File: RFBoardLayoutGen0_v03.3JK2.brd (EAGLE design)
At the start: 76.9 x 40.1 mm, 79 parts

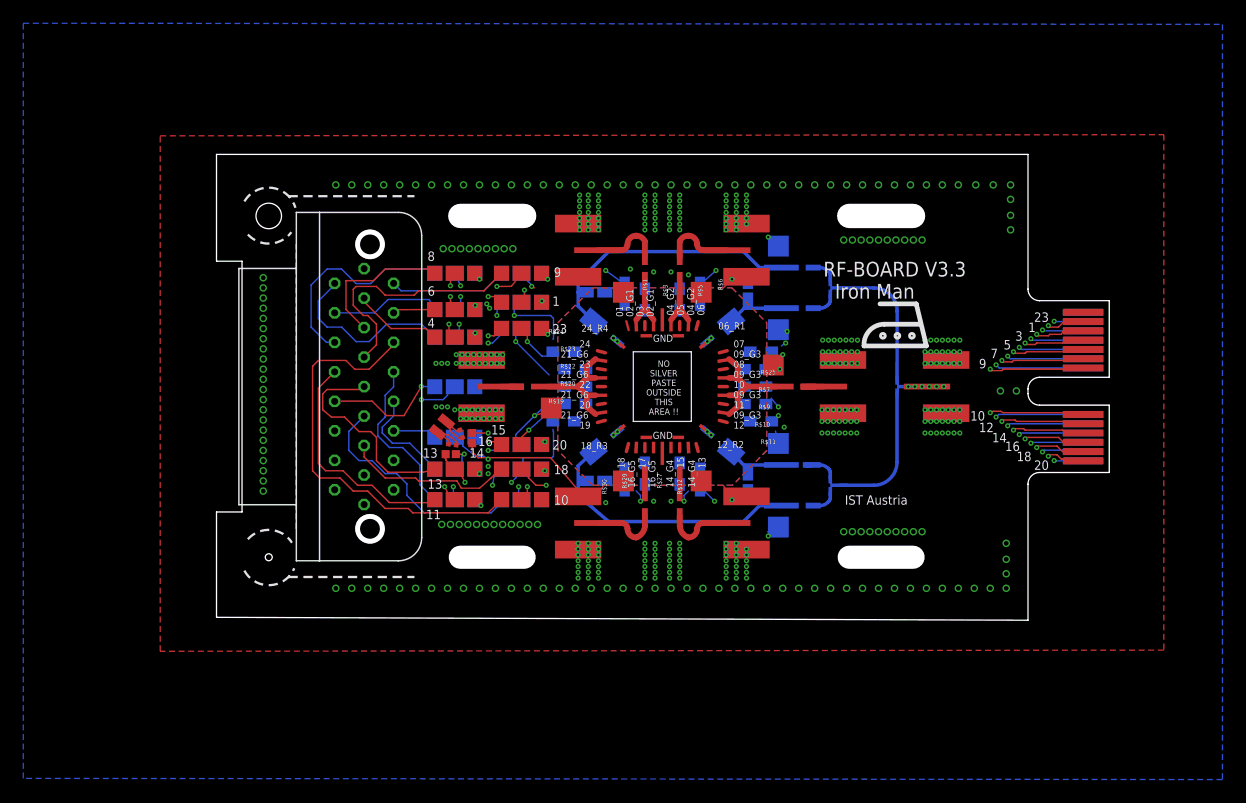
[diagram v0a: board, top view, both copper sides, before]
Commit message: moving border vias
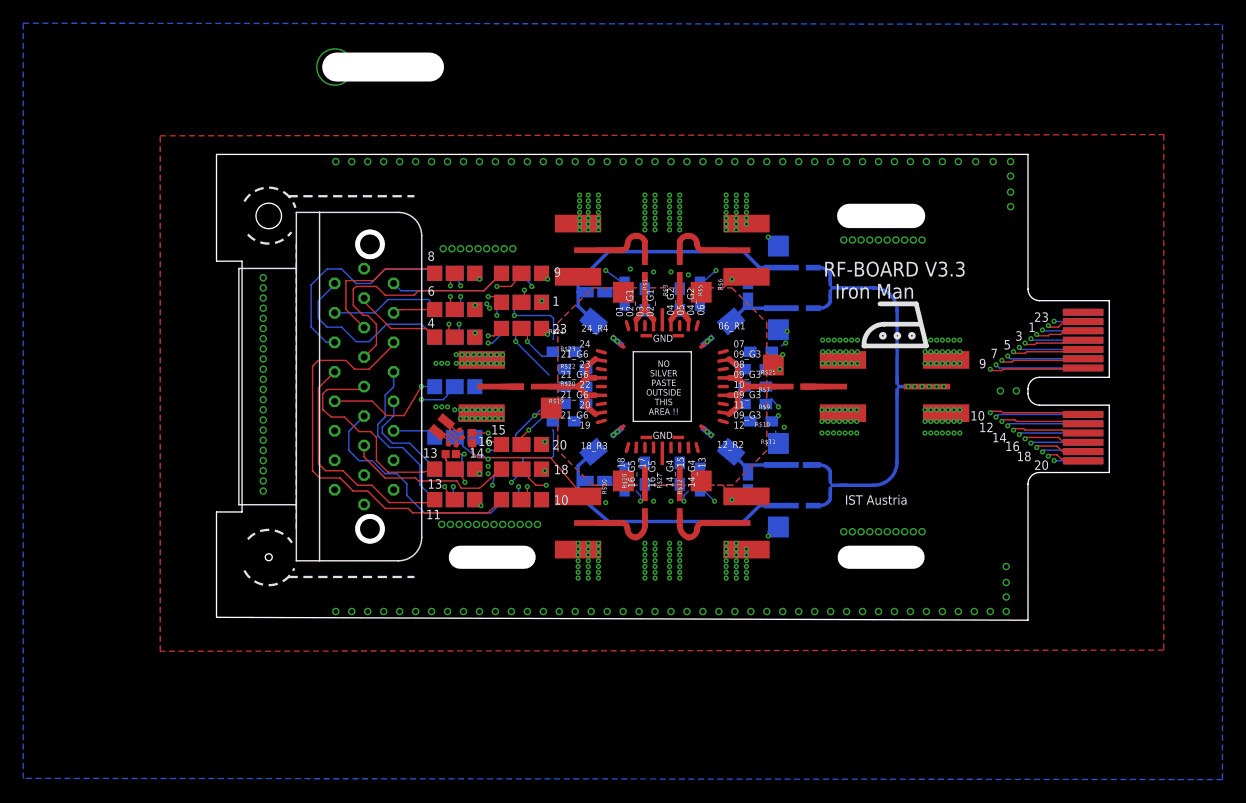
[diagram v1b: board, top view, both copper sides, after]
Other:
- board size 76.9 x 40.1 mm -> 76.9 x 47.6 mm

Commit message: added holes for blue fors
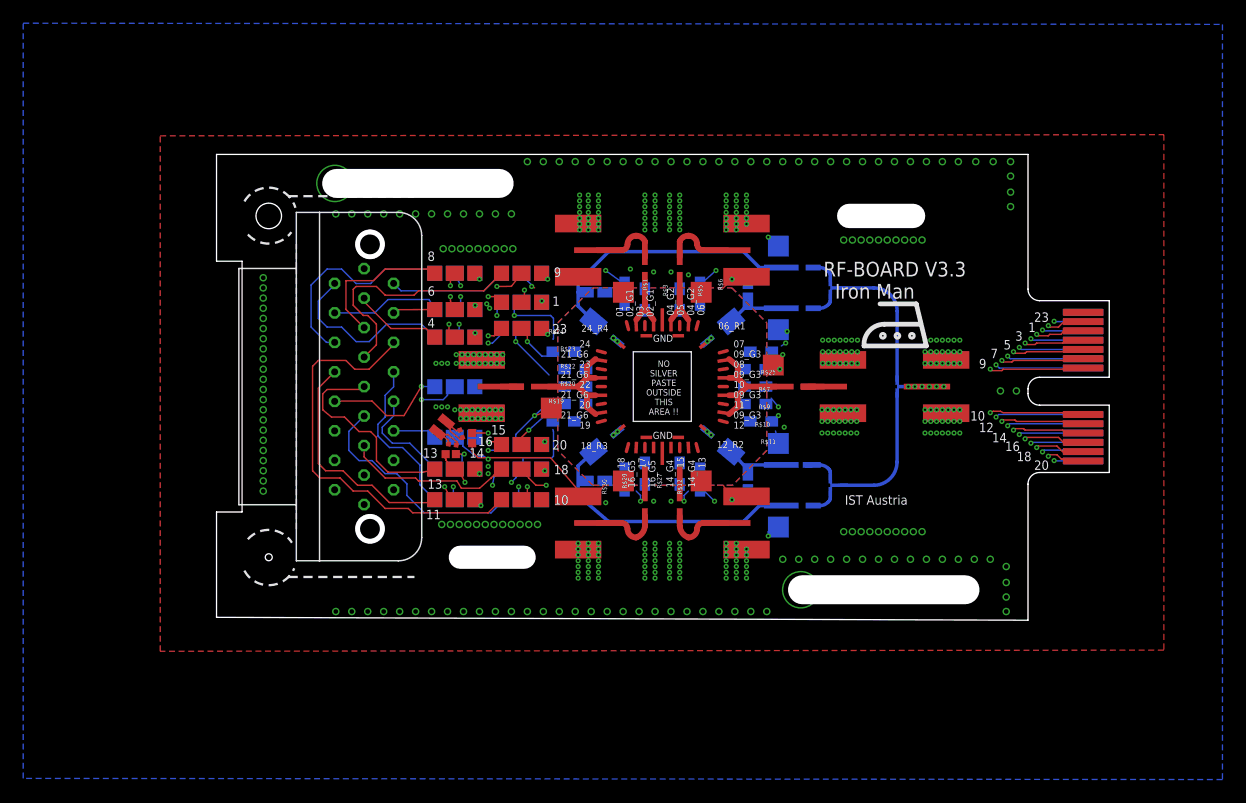
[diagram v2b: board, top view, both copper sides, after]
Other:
- board size 76.9 x 47.6 mm -> 76.9 x 40.1 mm
- board text added: "tell beta to put Cu on walls here"

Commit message: back two holes added
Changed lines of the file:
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@@
 <text x="-23.95" y="5.45" size="0.8128" layer="22" font="vector" ratio="15" rot="MR180">10</text>
 <text x="-26.5" y="1.6" size="0.8128" layer="22" font="vector" ratio="15" rot="MR180">13</text>
-<circle x="-33.9" y="14.7" radius="2" width="0" layer="29"/>
-<circle x="-33.9" y="-14.7" radius="2" width="0" layer="29"/>
 <wire x1="-36" y1="15.95" x2="-31.6" y2="15.4" width="0.2" layer="21" style="dashdot" curve="-133.254829"/>
 <wire x1="-35.7" y1="13.1" x2="-31.95" y2="13.3" width="0.2" layer="21" style="dashdot" curve="100.804892"/>
@@
 <circle x="-25.18125" y="-12.25" radius="1.05625" width="0.4064" layer="20"/>
 <circle x="-25.18125" y="12.25" radius="1.05625" width="0.4064" layer="20"/>
-<hole x="-33.9" y="-14.7" drill="0.6"/>
-<hole x="-33.9" y="14.7" drill="2.2"/>
 <wire x1="11.2" y1="13.29375" x2="12.64375" y2="11.39375" width="0.3048" layer="100"/>
 <wire x1="-7.70625" y1="13.3" x2="-10.275" y2="10.4" width="0.3048" layer="100"/>
@@
 <via x="29.625" y="-16.875" extent="1-16" drill="0.4"/>
 <via x="29.625" y="-15.5" extent="1-16" drill="0.4"/>
+<via x="-33.9" y="14.7" extent="1-16" drill="2.1" diameter="4"/>
 <wire x1="-10.4" y1="5.01" x2="-10.4" y2="5.01" width="0" layer="19" extent="1-16"/>
 <wire x1="-16.15" y1="-9.74" x2="-16.15" y2="-9.74" width="0" layer="19" extent="1-16"/>
+<via x="-33.9" y="-14.7" extent="1-16" drill="2.1" diameter="4"/>
 </signal>
 <signal name="N$5" class="2">
@@
 <via x="-28.2" y="17.5" extent="1-16" drill="3"/>
 <via x="-14.1" y="17.5" extent="1-16" drill="2.1"/>
+<wire x1="-14.1" y1="17.5" x2="-28.2" y2="17.5" width="0" layer="19" extent="1-1"/>
 </signal>
 <signal name="GND2">
 <via x="11.925" y="-17.5" extent="1-16" drill="3"/>
 <via x="26.025" y="-17.5" extent="1-16" drill="2.1"/>
+<wire x1="11.925" y1="-17.5" x2="26.025" y2="-17.5" width="0" layer="19" extent="1-1"/>
 </signal>
 </signals>

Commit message: Backup commit
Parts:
- added U$11, U$12, U$13, U$14: LP-FILTER/VARACTOR/0402, LPFilter:LP-FILTER/VARACTOR/0402
- moved R$27 1.50 mm to (0.00, -7.50)
- moved R$5 1.50 mm to (0.00, 7.50)
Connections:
- removed net $1234567254654: E$2.25, LP$1.$6, LP$10.$6, LP$11.$6, LP$12.$6, LP$13.$6, LP$14.$6, LP$15.$6, LP$16.$6, LP$17.$6, LP$18.$6, LP$19.$6, LP$2.$6, LP$20.$6, LP$21.$6, LP$22.$6, LP$23.$6, LP$24.$6, LP$3.$6, LP$4.$6, LP$5.$6, LP$6.$6, LP$7.$6, LP$8.$6, LP$9.$6, S$1.2@1, S$1.2@2, S$2.2@1, S$2.2@2, S$3.2@1, S$3.2@2, S$4.2@1, S$4.2@2, S$5.2@1, S$5.2@2, S$6.2@1, S$6.2@2, S$7.2@1, S$7.2@2, U$1.25, U$1.26
- net GND: now also E$2.25, LP$1.$6, LP$10.$6, LP$11.$6, LP$12.$6, LP$13.$6, LP$14.$6, LP$15.$6, LP$16.$6, LP$17.$6, LP$18.$6, LP$19.$6, LP$2.$6, LP$20.$6, LP$21.$6, LP$22.$6, LP$23.$6, LP$24.$6, LP$3.$6, LP$4.$6, LP$5.$6, LP$6.$6, LP$7.$6, LP$8.$6, LP$9.$6, S$1.2@1, S$1.2@2, S$2.2@1, S$2.2@2, S$3.2@1, S$3.2@2, S$4.2@1, S$4.2@2, S$5.2@1, S$5.2@2, S$6.2@1, S$6.2@2, S$7.2@1, S$7.2@2, U$1.25, U$1.26
- net N$10: now also U$14.IN
- net N$11: now also U$13.IN
- net N$2: now also U$12.IN
- net N$9: now also U$11.IN
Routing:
- added copper zone on layer 1, net GND
- added copper zone on layer 14, net GND
- added copper zone on layer 15, net GND
- added copper zone on layer 16, net GND
- added copper zone on layer 2, net GND
- added copper zone on layer 3, net GND
- removed copper zone on layer 1, net $1234567254654
- removed copper zone on layer 14, net $1234567254654
- removed copper zone on layer 15, net $1234567254654
- removed copper zone on layer 16, net $1234567254654
- removed copper zone on layer 2, net $1234567254654
- removed copper zone on layer 3, net $1234567254654

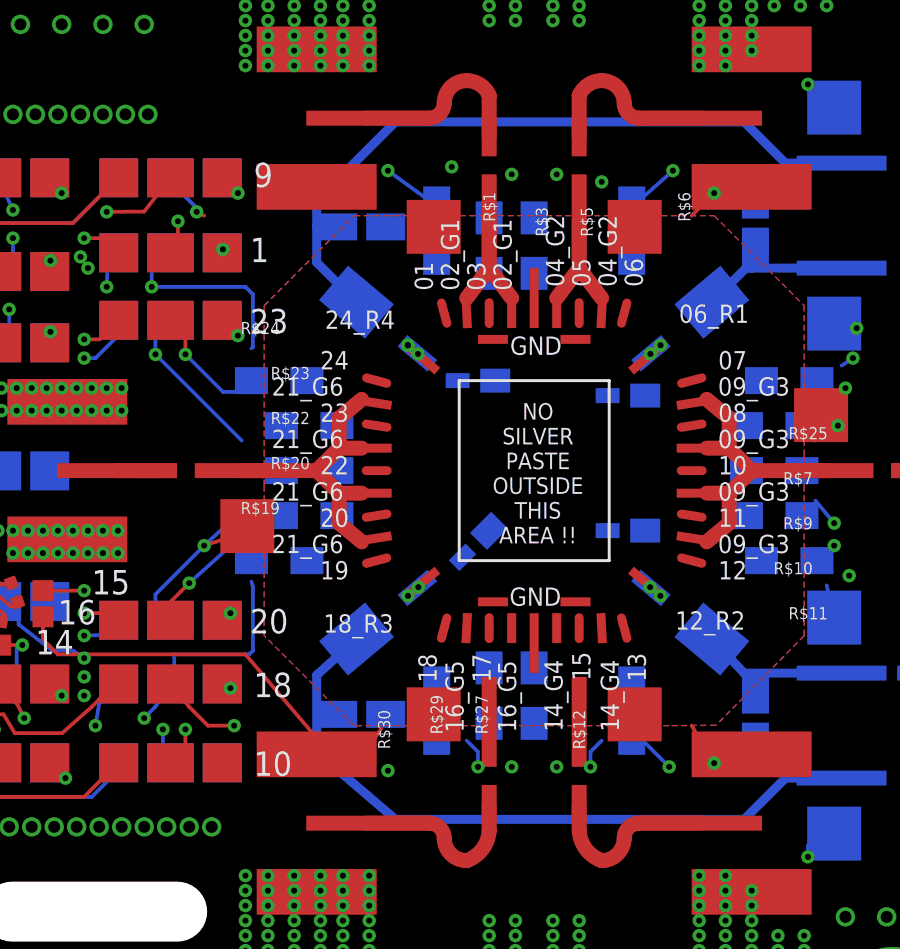
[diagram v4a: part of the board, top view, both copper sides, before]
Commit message: varactors added - problem spotted
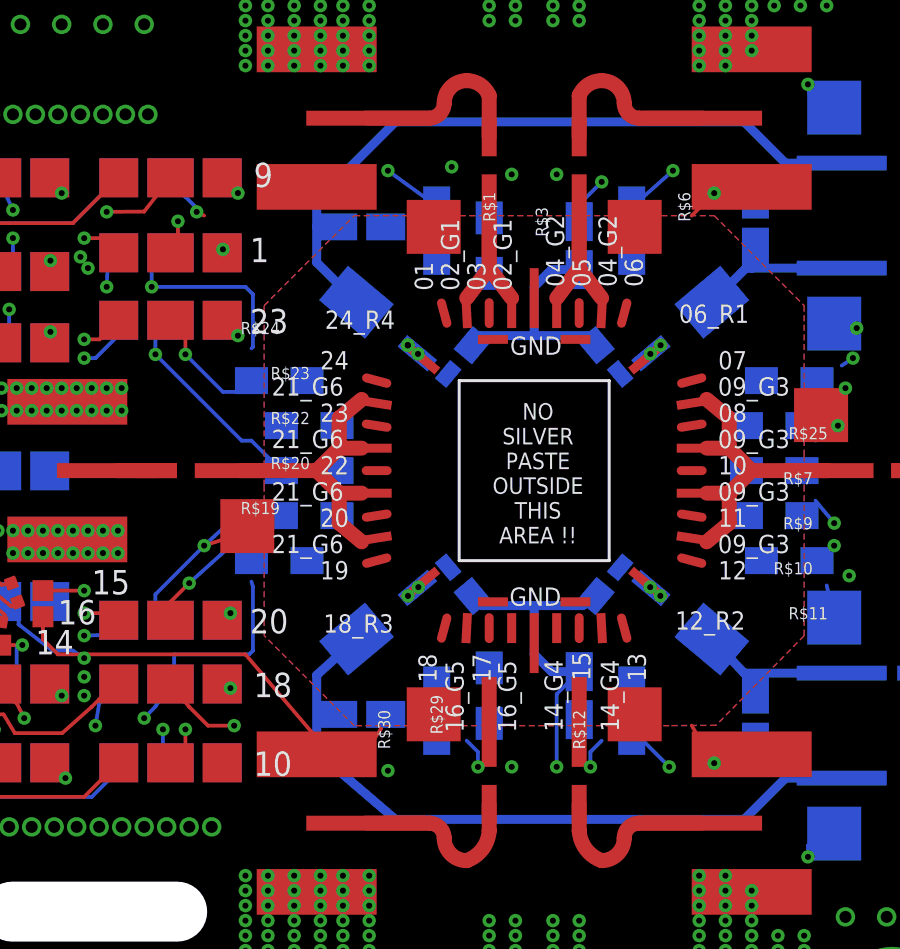
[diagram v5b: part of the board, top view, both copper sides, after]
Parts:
- removed R$27, R$5: 10K, LPFilter:LP-FILTER/RESISTOR/0603_BOTTOM
- added U$15, U$16: LP-FILTER/CAPACITOR/0603, LPFilter:LP-FILTER/CAPACITOR/0603_BOTTOM
- moved U$12 1.71 mm to (2.51, -3.64), turned to 230 degrees
- moved U$11 1.25 mm to (-2.51, -3.64), turned to 310 degrees
- moved U$13 1.24 mm to (2.51, 3.64), turned to 130 degrees
- moved U$14 0.82 mm to (-2.51, 3.64), turned to 50 degrees
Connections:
- removed net DC$15: R$27.OUT, U$6.DC§15
- removed net N$29: R$5.OUT, U$6.DC§05
- net D$15: now also U$11.OUT, U$12.OUT, U$16.OUT; no longer R$27.IN
- net D$5: now also U$13.OUT, U$14.OUT, U$15.OUT; no longer R$5.IN
- net GND: now also U$15.IN, U$16.IN
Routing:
- net D$15: track 70.2 -> 81.5 mm
- net D$5: track 65.4 -> 74.8 mm
- net D$22: track 61.9 -> 63.6 mm

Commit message: Routing
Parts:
- moved R$20 0.50 mm to (-8.00, -1.50)
- moved R$22 0.50 mm to (-8.00, 0.00)
- moved R$23 0.50 mm to (-8.00, 1.50)
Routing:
- net D$16: track 75.5 -> 69.1 mm, vias 3 -> 4
- net N$8: track 0.00 -> 5.12 mm
- net N$7: track 0.00 -> 5.12 mm
- net N$4: track 0.00 -> 2.43 mm, vias 0 -> 1
- net DC$24: track 0.00 -> 2.43 mm, vias 0 -> 1
- net DC$19: track 0.00 -> 2.43 mm, vias 0 -> 1
- net N$28: track 0.00 -> 2.39 mm, vias 0 -> 1
- net D$8: track 75.9 -> 78.1 mm
- net D$2: track 53.8 -> 55.8 mm
- net DC$6: track 0.00 -> 1.87 mm, vias 0 -> 1
- net DC$1: track 0.00 -> 1.87 mm, vias 0 -> 1
- net N$31: track 0.00 -> 1.86 mm, vias 0 -> 1
- net DC$13: track 0.00 -> 1.86 mm, vias 0 -> 1
- net N$33: track 0.00 -> 1.83 mm, vias 0 -> 1
- net N$32: track 0.00 -> 1.83 mm, vias 0 -> 1
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
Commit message: Backup commit
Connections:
- net GND: now also U$6.GND$1, U$6.GND$2, U$6.GND$3, U$6.GND$4, U$6.GND$5, U$6.GND$6
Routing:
- net D$3: track 63.3 -> 63.9 mm
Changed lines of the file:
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@@
 <signal name="D$3">
 <contactref element="LP$9" pad="$4"/>
-<via x="-0.75" y="9.875" extent="1-16" drill="0.2"/>
-<wire x1="-0.75" y1="9.875" x2="-1.25" y2="9.375" width="0.125" layer="14"/>
-<wire x1="-1.25" y1="9.375" x2="-6.5" y2="9.375" width="0.125" layer="14"/>
+<via x="-0.625" y="10.375" extent="1-16" drill="0.2"/>
+<wire x1="-0.625" y1="10.375" x2="-1.375" y2="9.375" width="0.125" layer="14"/>
+<wire x1="-1.375" y1="9.375" x2="-6.5" y2="9.375" width="0.125" layer="14"/>
 <wire x1="-6.5" y1="9.375" x2="-11" y2="4.875" width="0.125" layer="14"/>
 <wire x1="-11" y1="4.875" x2="-14.25" y2="4.875" width="0.125" layer="14"/>
@@
 <wire x1="25.125" y1="9.25" x2="8.625" y2="9.25" width="0.125" layer="3"/>
 <wire x1="8.625" y1="9.25" x2="7.125" y2="10.75" width="0.125" layer="3"/>
-<wire x1="7.125" y1="10.75" x2="0" y2="10.75" width="0.125" layer="3"/>
-<wire x1="0" y1="10.75" x2="-0.75" y2="9.875" width="0.125" layer="3"/>
+<wire x1="7.125" y1="10.75" x2="-0.375" y2="10.75" width="0.125" layer="3"/>
+<wire x1="-0.375" y1="10.75" x2="-0.625" y2="10.375" width="0.125" layer="3"/>
 <contactref element="R$3" pad="IN"/>
-<wire x1="-1.5" y1="8.425" x2="-1.5" y2="9.125" width="0.125" layer="16"/>
-<wire x1="-1.5" y1="9.125" x2="-0.75" y2="9.875" width="0.125" layer="16"/>
+<wire x1="-1.5" y1="8.425" x2="-1.5" y2="9.2125" width="0.125" layer="16"/>
+<wire x1="-1.5" y1="9.2125" x2="-0.625" y2="10.375" width="0.125" layer="16"/>
 </signal>
 <signal name="D$4">
 <contactref element="LP$3" pad="$4"/>
-<via x="0.75" y="9.875" extent="1-16" drill="0.2"/>
-<wire x1="0.75" y1="9.875" x2="0.25" y2="9.125" width="0.125" layer="14"/>
-<wire x1="0.25" y1="9.125" x2="-0.625" y2="9.125" width="0.125" layer="14"/>
+<via x="0.125" y="10.375" extent="1-16" drill="0.2"/>
 <via x="-18.375" y="5.375" extent="1-16" drill="0.2"/>
 <wire x1="-18.375" y1="5.375" x2="-18.375" y2="4.5" width="0.125" layer="1"/>
 <wire x1="-18.375" y1="4.5" x2="-18.5" y2="3.76" width="0.125" layer="1"/>
 <wire x1="-18.5" y1="3.76" x2="-17.875" y2="4.26" width="0.125" layer="1"/>
-<wire x1="-0.625" y1="9.125" x2="-0.75" y2="9" width="0.125" layer="14"/>
-<wire x1="-0.75" y1="9" x2="-6.375" y2="9" width="0.125" layer="14"/>
+<wire x1="-1.125" y1="9" x2="-6.375" y2="9" width="0.125" layer="14"/>
 <wire x1="-6.375" y1="9" x2="-10.75" y2="4.375" width="0.125" layer="14"/>
 <wire x1="-10.75" y1="4.375" x2="-14.25" y2="4.375" width="0.125" layer="14"/>
@@
 <wire x1="4.75" y1="9.5" x2="5.25" y2="10" width="0.125" layer="3"/>
 <wire x1="5.25" y1="10" x2="7.375" y2="10" width="0.125" layer="3"/>
-<wire x1="1.25" y1="10.375" x2="0.75" y2="9.875" width="0.125" layer="3"/>
 <contactref element="B$2" pad="LF"/>
-<wire x1="1.25" y1="10.375" x2="3.375" y2="10.375" width="0.125" layer="3"/>
+<wire x1="0.125" y1="10.375" x2="3.375" y2="10.375" width="0.125" layer="3"/>
 <wire x1="3.375" y1="10.375" x2="3.625" y2="10.375" width="0.125" layer="3"/>
 <wire x1="3.625" y1="10.375" x2="4.5" y2="9.5" width="0.125" layer="3"/>
@@
 <via x="3.375" y="9.875" extent="1-16" drill="0.2"/>
 <wire x1="3.375" y1="9.875" x2="3.375" y2="10.375" width="0.125" layer="3"/>
+<wire x1="-1.125" y1="9" x2="0.125" y2="10.25" width="0.125" layer="14"/>
+<wire x1="0.125" y1="10.25" x2="0.125" y2="10.375" width="0.125" layer="14"/>
 </signal>
 <signal name="D$5">
 <contactref element="LP$8" pad="$4"/>
 <via x="2.25" y="9.625" extent="1-16" drill="0.2"/>
-<wire x1="2.25" y1="9.625" x2="1.25" y2="10.625" width="0.125" layer="14"/>
-<wire x1="1.25" y1="10.625" x2="-1.875" y2="10.625" width="0.125" layer="14"/>
-<wire x1="-1.875" y1="10.625" x2="-2.125" y2="10.875" width="0.125" layer="14"/>
-<wire x1="-2.125" y1="10.875" x2="-10" y2="10.875" width="0.125" layer="14"/>
+<wire x1="2.25" y1="9.625" x2="1.125" y2="10.875" width="0.125" layer="14"/>
+<wire x1="1.125" y1="10.875" x2="-10" y2="10.875" width="0.125" layer="14"/>
 <wire x1="-10" y1="10.875" x2="-12.625" y2="8.25" width="0.125" layer="14"/>
 <wire x1="-12.625" y1="8.25" x2="-12.625" y2="7.625" width="0.125" layer="14"/>
@@
 <contactref element="U$15" pad="IN"/>
 <contactref element="U$16" pad="IN"/>
+<contactref element="U$6" pad="GND$3"/>
+<contactref element="U$6" pad="GND$1"/>
+<contactref element="U$6" pad="GND$4"/>
+<contactref element="U$6" pad="GND$6"/>
+<contactref element="U$6" pad="GND$5"/>
+<contactref element="U$6" pad="GND$2"/>
 <wire x1="7.25" y1="9.4575" x2="7.375" y2="9.05" width="0" layer="19" extent="1-16"/>
 <wire x1="-10.4" y1="5.01" x2="-10.4" y2="5.01" width="0" layer="19" extent="1-16"/>
@@
 <wire x1="-4.95" y1="-8.125" x2="-7.25" y2="-9.4575" width="0" layer="19" extent="1-16"/>
 <wire x1="-4.95" y1="8.125" x2="-7.25" y2="9.4575" width="0" layer="19" extent="1-16"/>
-<wire x1="1.5" y1="-8.3" x2="7.25" y2="-9.4575" width="0" layer="19" extent="1-16"/>
-<wire x1="1.5" y1="8.3" x2="7.25" y2="9.4575" width="0" layer="19" extent="1-16"/>
+<wire x1="-1.375" y1="4.375" x2="-4.95" y2="8.125" width="0" layer="19" extent="1-16"/>
+<wire x1="0" y1="5.75" x2="-1.375" y2="4.375" width="0" layer="19" extent="1-1"/>
+<wire x1="1.375" y1="4.375" x2="0" y2="5.75" width="0" layer="19" extent="1-1"/>
+<wire x1="1.5" y1="8.3" x2="0" y2="5.75" width="0" layer="19" extent="1-16"/>
+<wire x1="-1.375" y1="-4.375" x2="-4.95" y2="-8.125" width="0" layer="19" extent="1-16"/>
+<wire x1="0" y1="-5.75" x2="-1.375" y2="-4.375" width="0" layer="19" extent="1-1"/>
+<wire x1="1.375" y1="-4.375" x2="0" y2="-5.75" width="0" layer="19" extent="1-1"/>
+<wire x1="1.5" y1="-8.3" x2="0" y2="-5.75" width="0" layer="19" extent="1-16"/>
 </signal>
 <signal name="N$18" class="2">

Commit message: Seems routed
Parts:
- moved U$15 1.35 mm to (0.25, 8.00)
- moved U$16 1.35 mm to (0.25, -8.00)
- moved U$8 0.62 mm to (-5.75, -8.75)
- moved U$7 0.50 mm to (-5.75, 8.62)
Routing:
- net GND: track 0.00 -> 8.25 mm, vias 485 -> 505
- net N$9: track 0.00 -> 1.39 mm
- net N$2: track 0.00 -> 1.38 mm
- net N$10: track 0.00 -> 1.36 mm
- net N$11: track 0.00 -> 1.31 mm
- net N$13: track 4.82 -> 5.89 mm
- net D$18: track 56.9 -> 58.0 mm
- net D$7: track 73.2 -> 74.2 mm
- net D$9: track 79.0 -> 80.0 mm
- net D$17: track 58.0 -> 57.1 mm
- net D$16: track 69.1 -> 69.8 mm
- net D$4: track 66.2 -> 66.8 mm
- net D$5: track 76.6 -> 77.2 mm
